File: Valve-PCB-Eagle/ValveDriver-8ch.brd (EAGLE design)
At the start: 101.6 x 66 mm, 21 parts, among them IC1 ULQ2803A, J10 Valve 3, J11 Valve 2, J12 Valve 1, J4 POWER_JACK, J5 Valve 8, J6 Valve 7, J7 Valve 6, J8 Valve 5, J9 Valve 4

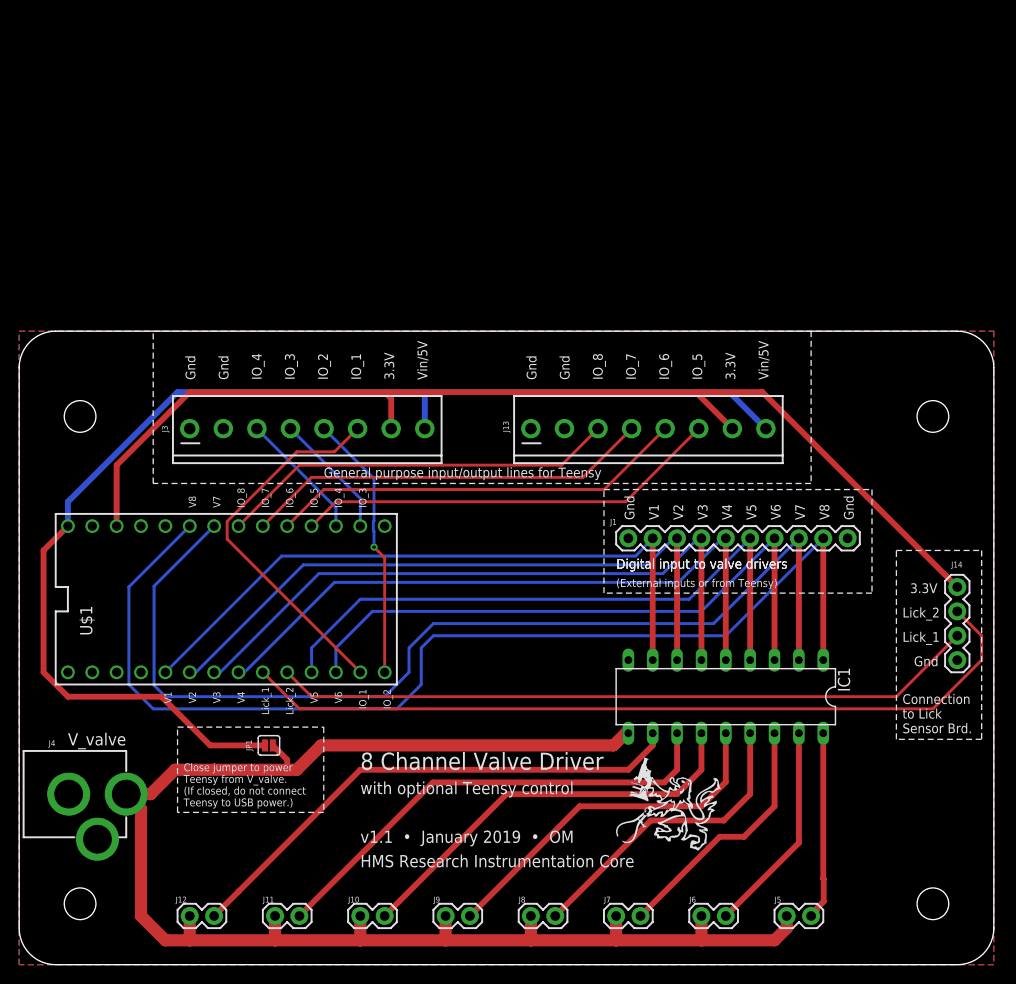
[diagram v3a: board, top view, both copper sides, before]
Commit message: [Valve] Add valve manifold connection
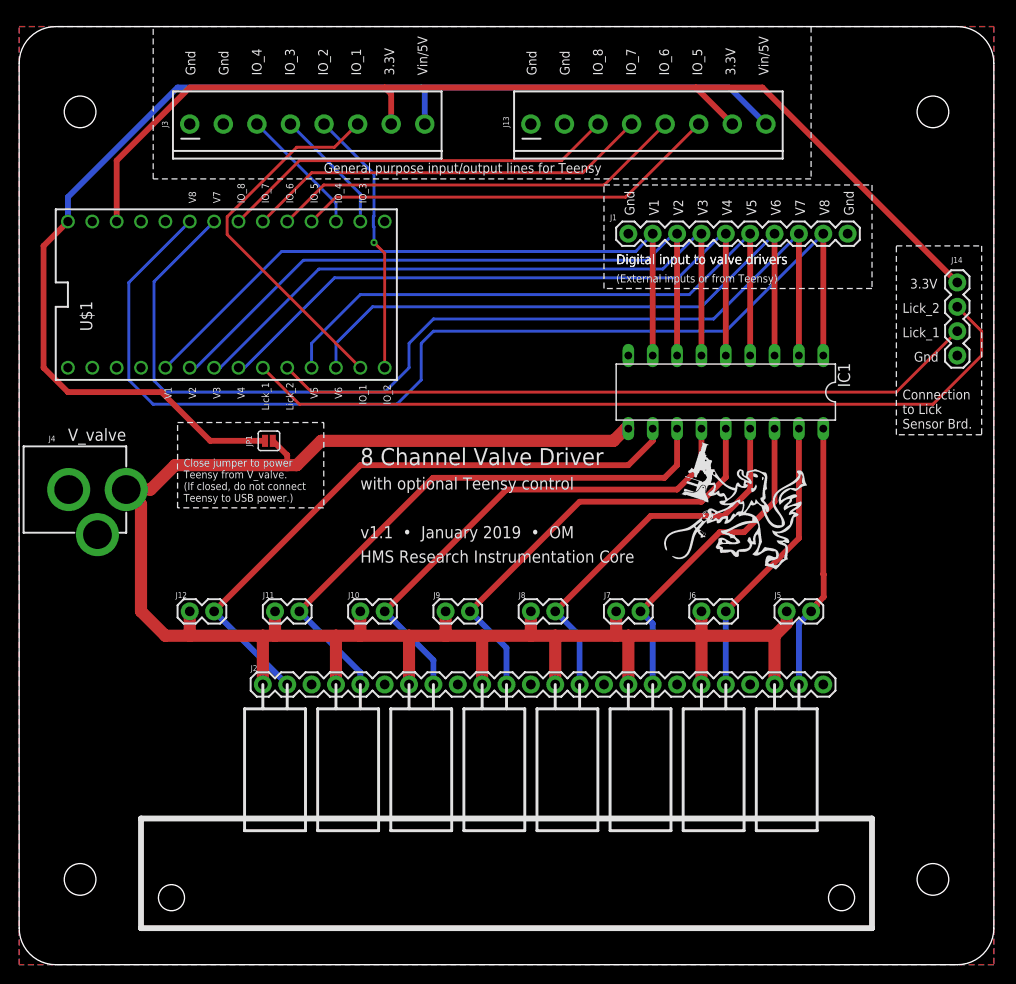
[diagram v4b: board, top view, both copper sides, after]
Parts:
- removed U$3: (no value), ofer-eagle-lib:RIC_LOGO_MED
- added J2: (no value), SparkFun-Connectors:1X24
- added U$7: (no value), ofer-eagle-lib:RIC_LOGO_BIG
- moved U$2 31.8 mm to (95.2, 88.9)
- moved U$6 31.8 mm to (6.35, 88.9)
- moved J1 31.8 mm to (63.5, 76.2)
- moved J10 31.8 mm to (35.6, 36.8)
- moved J11 31.8 mm to (26.7, 36.8)
- moved J12 31.8 mm to (17.8, 36.8)
- moved J14 31.8 mm to (97.8, 63.5)
- moved J4 31.8 mm to (-2.54, 49.5)
- moved J5 31.8 mm to (80.0, 36.8)
- moved J6 31.8 mm to (71.1, 36.8)
- moved J7 31.8 mm to (62.2, 36.8)
- moved J8 31.8 mm to (53.3, 36.8)
- moved J9 31.8 mm to (44.5, 36.8)
- moved JP1 31.8 mm to (26.0, 54.6)
- moved IC1 31.7 mm to (73.7, 59.7)
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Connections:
- removed net N$1: IC1.18, J5.2
- removed net N$2: IC1.17, J6.2
- removed net N$3: IC1.16, J7.2
- removed net N$4: IC1.15, J8.2
- removed net N$5: IC1.14, J9.2
- removed net N$6: IC1.13, J10.2
- removed net N$7: IC1.12, J11.2
- removed net N$8: IC1.11, J12.2
- new net V1OUT: IC1.11, J12.2, J2.3
- new net V2OUT: IC1.12, J11.2, J2.6
- new net V3OUT: IC1.13, J10.2, J2.9
- new net V4OUT: IC1.14, J2.12, J9.2
- new net V5OUT: IC1.15, J2.15, J8.2
- new net V6OUT: IC1.16, J2.18, J7.2
- new net V7OUT: IC1.17, J2.21, J6.2
- new net V8OUT: IC1.18, J2.24, J5.2
- net V_VALVE: now also J2.11, J2.14, J2.17, J2.2, J2.20, J2.23, J2.5, J2.8
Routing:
- net V1OUT: track 0.00 -> 65.1 mm
- net V2OUT: track 0.00 -> 59.7 mm
- net N$8: track 54.4 -> 0.00 mm
- net V3OUT: track 0.00 -> 52.9 mm
- net N$7: track 49.5 -> 0.00 mm
- net V4OUT: track 0.00 -> 46.7 mm
- net N$6: track 43.1 -> 0.00 mm
- net V_VALVE: track 159.4 -> 200.0 mm
- net V5OUT: track 0.00 -> 40.6 mm
- net N$5: track 37.5 -> 0.00 mm
- net V6OUT: track 0.00 -> 34.5 mm
- net N$4: track 31.9 -> 0.00 mm
- net V7OUT: track 0.00 -> 29.8 mm
- net V8OUT: track 0.00 -> 27.8 mm
- net N$3: track 26.3 -> 0.00 mm
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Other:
- board size 101.6 x 66 mm -> 101.6 x 97.8 mm

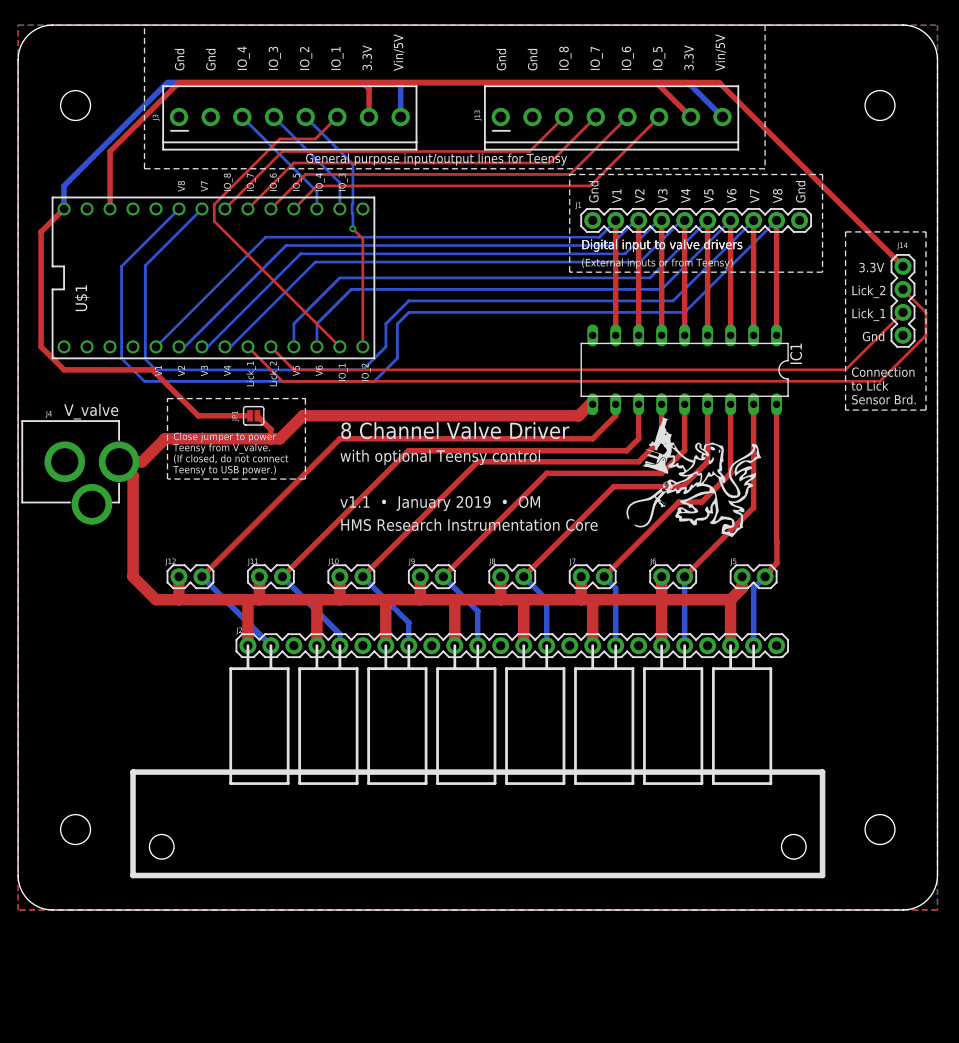
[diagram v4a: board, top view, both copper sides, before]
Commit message: [Valve] Add momentary push buttons (fixes #1)
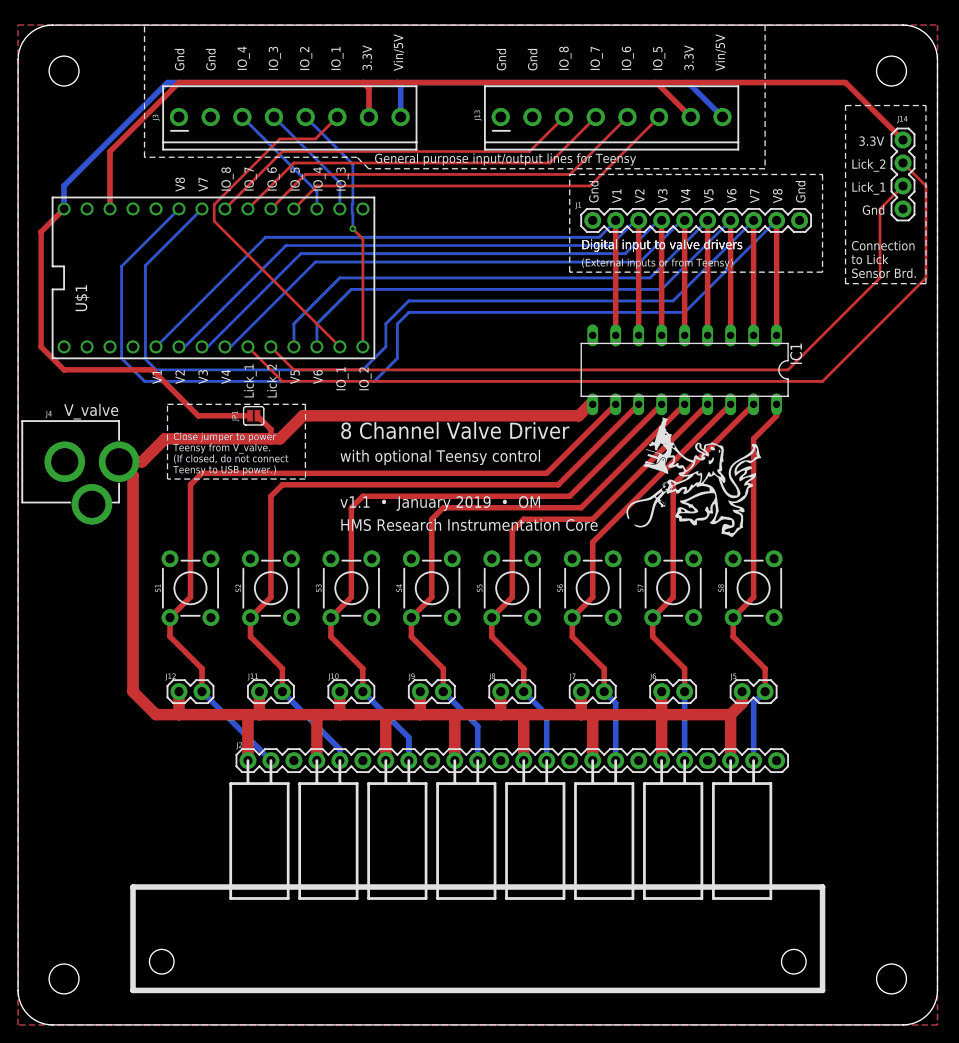
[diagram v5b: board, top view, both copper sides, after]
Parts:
- added S1, S2, S3, S4, S5, S6, S7, S8: MOMENTARY-SWITCH-SPST-PTH-6.0MM, SparkFun-Switches:TACTILE_SWITCH_PTH_6.0MM
- moved U$4 16.6 mm to (96.5, -7.62)
- moved U$5 16.6 mm to (5.08, -7.62)
- moved J14 14.0 mm to (97.8, 77.5)
- moved J10 12.7 mm to (35.6, 24.1)
- moved J11 12.7 mm to (26.7, 24.1)
- moved J12 12.7 mm to (17.8, 24.1)
- moved J2 12.7 mm to (52.1, 16.5)
- moved J5 12.7 mm to (80.0, 24.1)
- moved J6 12.7 mm to (71.1, 24.1)
- moved J7 12.7 mm to (62.2, 24.1)
- moved J8 12.7 mm to (53.3, 24.1)
- moved J9 12.7 mm to (44.5, 24.1)
- moved U$6 4.02 mm to (5.08, 92.7)
- moved U$2 4.02 mm to (96.5, 92.7)
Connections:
- net GND: now also S1.3, S2.3, S3.3, S4.3, S5.3, S6.3, S7.3, S8.3
- net V1OUT: now also S1.1
- net V2OUT: now also S2.1
- net V3OUT: now also S3.1
- net V4OUT: now also S4.1
- net V5OUT: now also S5.1
- net V6OUT: now also S6.1
- net V7OUT: now also S7.1
- net V8OUT: now also S8.1
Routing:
- net V1OUT: track 65.1 -> 86.7 mm
- net V2OUT: track 59.7 -> 79.1 mm
- net V3OUT: track 52.9 -> 71.5 mm
- net V4OUT: track 46.7 -> 63.8 mm
- net V5OUT: track 40.6 -> 56.2 mm
- net V7OUT: track 29.8 -> 45.5 mm
- net V8OUT: track 27.8 -> 43.3 mm
- net V6OUT: track 34.5 -> 48.6 mm
- net V_VALVE: track 200.0 -> 212.7 mm
- net LICK_2: track 84.7 -> 95.0 mm
- net LICK_1: track 73.5 -> 83.8 mm
- net 3.3V: track 115.0 -> 109.2 mm
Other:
- board size 101.6 x 97.8 mm -> 101.6 x 110.5 mm

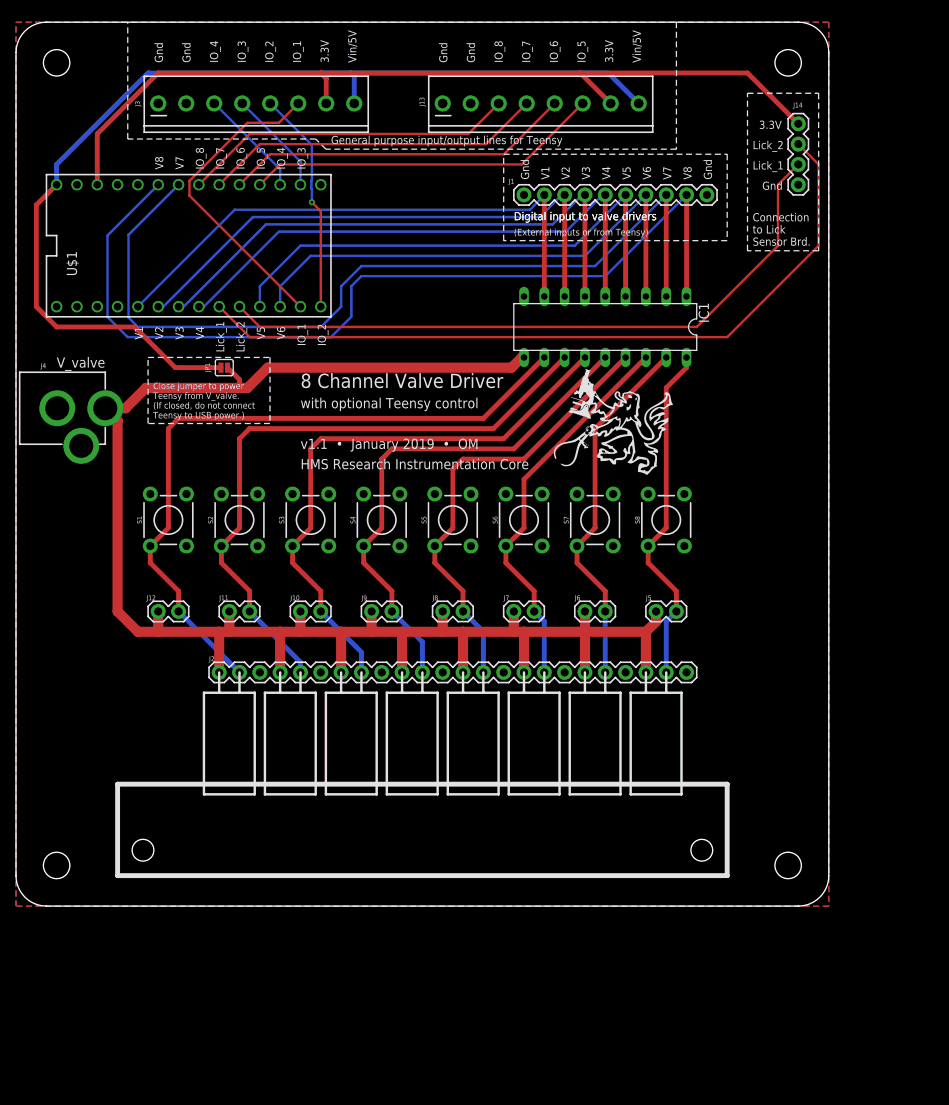
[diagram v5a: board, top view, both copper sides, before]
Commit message: [Valve] Silkscreen improvements
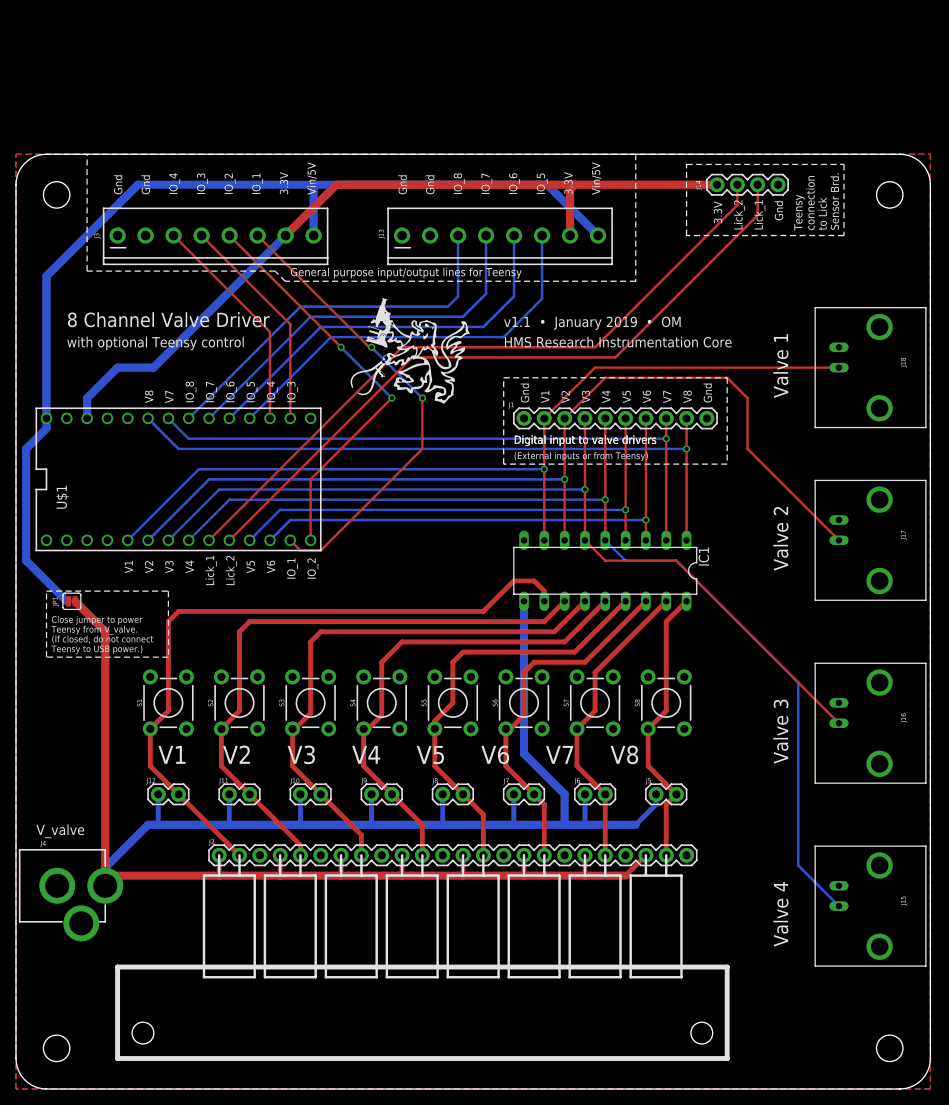
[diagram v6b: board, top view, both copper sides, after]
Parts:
- added J15, J16, J17, J18: BNCPTH, SparkFun-Connectors:BNC
- moved J4 59.7 mm to (-2.54, -10.2)
- moved JP1 34.9 mm to (6.99, 25.4)
- moved IC1 30.5 mm to (73.7, 29.2)
- moved U$1 29.2 mm to (20.3, 40.6)
- moved J1 27.9 mm to (63.5, 48.3)
- moved U$7 26.9 mm to (49.5, 55.9)
- moved U$4 26.2 mm to (109.2, -30.5)
- moved S1 22.9 mm to (19.1, 12.7)
- moved S2 22.9 mm to (27.9, 12.7)
- moved S3 22.9 mm to (36.8, 12.7)
- moved S4 22.9 mm to (45.7, 12.7)
- moved S5 22.9 mm to (54.6, 12.7)
- moved S6 22.9 mm to (63.5, 12.7)
- moved S7 22.9 mm to (72.4, 12.7)
- moved S8 22.9 mm to (81.3, 12.7)
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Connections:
- net GND: now also J15.GND, J16.GND, J17.GND, J18.GND
- net V1: now also J18.S
- net V2: now also J17.S
- net V3: now also J16.S
- net V4: now also J15.S
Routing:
- net V4: track 69.3 -> 131.0 mm, vias 0 -> 1
- net V2: track 69.3 -> 119.0 mm, vias 0 -> 1
- net V_VALVE: track 212.7 -> 256.4 mm
- net V3: track 69.3 -> 111.2 mm, vias 0 -> 1
- net V1: track 69.3 -> 110.5 mm, vias 0 -> 1
- net V8: track 114.9 -> 84.1 mm, vias 0 -> 1
- net V7: track 107.9 -> 78.5 mm, vias 0 -> 1
- net IO_2: track 28.1 -> 50.7 mm, vias 1 -> 2
- net IO_1: track 39.1 -> 57.7 mm, vias 0 -> 2
- net IO_3: track 13.2 -> 27.5 mm
- net IO_4: track 13.6 -> 27.9 mm
- net 3.3V: track 109.2 -> 98.9 mm
- net LICK_2: track 95.0 -> 85.9 mm
- net V8OUT: track 43.3 -> 35.7 mm
- net V7OUT: track 45.5 -> 37.8 mm
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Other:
- board size 101.6 x 110.5 mm -> 114.3 x 116.8 mm
- board text added: "Teensy connection to Lick Sensor Brd."
- board text added: "V1 V2 V3 V4 V5 V6 V7 V8"
- board text added: "Valve 1"
- board text added: "Valve 2"
- board text added: "Valve 3"
- board text added: "Valve 4"
- board text removed: "Connection to Lick Sensor Brd."

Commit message: [Valve] Remove manifold; remove buttons 5–8; make PCB more compact
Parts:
- removed J13: (no value), SparkFun-Connectors:SCREWTERMINAL-3.5MM-8
- removed J14: (no value), SparkFun-Connectors:1X04
- removed J2: (no value), SparkFun-Connectors:1X24
- removed S5, S6, S7, S8: MOMENTARY-SWITCH-SPST-PTH-6.0MM, SparkFun-Switches:TACTILE_SWITCH_PTH_6.0MM
- J3: device SparkFun-Connectors:SCREWTERMINAL-3.5MM-8 -> SparkFun-Connectors:1X08
- moved J18 87.0 mm to (16.5, 64.8), turned to 0 degrees
- moved J15 79.5 mm to (85.1, 64.8), turned to 0 degrees
- moved J17 71.0 mm to (39.4, 64.8), turned to 0 degrees
- moved J16 68.1 mm to (62.2, 64.8), turned to 0 degrees
- moved S4 56.6 mm to (86.4, 52.1), turned to 0 degrees
- moved S3 47.6 mm to (63.5, 52.1), turned to 0 degrees
- moved J3 45.8 mm to (50.8, 45.7), turned to 270 degrees
- moved U$7 42.3 mm to (81.3, 27.9)
- moved S2 41.0 mm to (39.4, 52.1), turned to 0 degrees
- moved S1 39.6 mm to (15.2, 52.1), turned to 0 degrees
- moved U$4 37.8 mm to (96.5, 5.08)
- moved U$5 35.6 mm to (5.08, 5.08)
- moved J4 26.7 mm to (-2.54, 16.5)
- moved IC1 24.0 mm to (53.3, 16.5)
- moved U$2 13.7 mm to (96.5, 71.1)
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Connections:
- removed net IO_5: J13.6, U$1.16/A2
- removed net IO_6: J13.5, U$1.17/A3
- removed net IO_7: J13.4, U$1.18/A4
- removed net IO_8: J13.3, U$1.19/A5
- removed net LICK_1: J14.2, U$1.8
- removed net LICK_2: J14.3, U$1.7
- net 3.3V: no longer J13.7, J14.4
- net GND: no longer J13.1, J13.2, J14.1, S5.3, S6.3, S7.3, S8.3
- net V1OUT: no longer J2.3
- net V2OUT: no longer J2.6
- net V3OUT: no longer J2.9
- net V4OUT: no longer J2.12
- net V5OUT: no longer J2.15, S5.1
- net V6OUT: no longer J2.18, S6.1
- net V7OUT: no longer J2.21, S7.1
- net V8OUT: no longer J2.24, S8.1
- net V_IN_TEENSY: no longer J13.8
- net V_VALVE: no longer J2.11, J2.14, J2.17, J2.2, J2.20, J2.23, J2.5, J2.8
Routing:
- net V_VALVE: track 256.4 -> 110.4 mm
- net LICK_1: track 86.7 -> 0.00 mm
- net LICK_2: track 85.9 -> 0.00 mm
- net V_IN_TEENSY: track 126.6 -> 74.0 mm
- net 3.3V: track 98.9 -> 47.9 mm
- net IO_5: track 50.6 -> 0.00 mm
- net IO_6: track 49.5 -> 0.00 mm
- net IO_7: track 48.4 -> 0.00 mm
- net IO_8: track 47.6 -> 0.00 mm
- net V5OUT: track 52.3 -> 9.72 mm
- net IO_1: track 57.7 -> 22.5 mm, vias 2 -> 1
- net IO_2: track 50.7 -> 18.9 mm, vias 2 -> 1
- net V6OUT: track 45.3 -> 15.1 mm
- net V4: track 131.0 -> 101.7 mm, vias 1 -> 2
- net V8: track 84.1 -> 108.1 mm
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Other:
- board size 114.3 x 116.8 mm -> 101.6 x 76.2 mm
- board text added: "V1 V2 V3 V4 V5 V6 IO_1 IO_2"
- board text added: "V8 V7 IO_4 IO_3"
- board text added: "v1.2 • Feb 2023 • OM"
- board text removed: "3.3V Lick_2 Lick_1 Gnd"
- board text removed: "Gnd Gnd IO_8 IO_7 IO_6 IO_5 3.3V Vin/5V"
- board text removed: "Teensy connection to Lick Sensor Brd."
- board text removed: "V1 V2 V3 V4 Lick_1 Lick_2 V5 V6 IO_1 IO_2"
- board text removed: "V8 V7 IO_8 IO_7 IO_6 IO_5 IO_4 IO_3"
- board text removed: "v1.1 • January 2019 • OM"
